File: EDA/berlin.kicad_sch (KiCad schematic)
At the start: 615 parts, among them J1 TYPE-C-31-M12_13, J2 Conn_ARM_JTAG_SWD_10, SW1,1 Rotary_Encoder_Switch_Chassis, SW1,10 MXSwitch, SW1,11 MXSwitch, SW1,12 MXSwitch, SW1,13 MXSwitch, SW1,14 MXSwitch, SW1,15 MXSwitch, SW1,16 Rotary_Encoder_Switch_Chassis, SW1,2 MXSwitch, SW1,3 MXSwitch, SW1,4 MXSwitch, SW1,5 MXSwitch, SW1,6 MXSwitch, SW1,7 MXSwitch, SW1,8 MXSwitch, SW1,9 MXSwitch, SW2,1 MXSwitch, SW2,10 MXSwitch, SW2,11 MXSwitch, SW2,12 MXSwitch, SW2,13 MXSwitch, SW2,14 MXSwitch, SW2,15 MXSwitch, SW2,16 MXSwitch, SW2,17 MXSwitch, SW2,18 MXSwitch, SW2,19 MXSwitch, SW2,2 MXSwitch, SW2,3 MXSwitch, SW2,4 MXSwitch, SW2,5 MXSwitch, SW2,6 MXSwitch, SW2,7 MXSwitch, SW2,9 MXSwitch, SW20-7,3 MXSwitch, SW3,1 MXSwitch, SW3,10 MXSwitch, SW3,11 MXSwitch, SW3,12 MXSwitch, SW3,13 MXSwitch, SW3,14 MXSwitch, SW3,15 MXSwitch, SW3,16 MXSwitch, SW3,17 MXSwitch, SW3,18 MXSwitch, SW3,19 MXSwitch, SW3,2 MXSwitch, SW3,3 MXSwitch, SW3,4 MXSwitch, SW3,5 MXSwitch, SW3,6 MXSwitch, SW3,7 MXSwitch, SW3,8 MXSwitch, SW3,9 MXSwitch, SW39-7,6 MXSwitch, SW4,1 MXSwitch, SW4,10 MXSwitch, SW4,11 MXSwitch, SW4,12 MXSwitch, SW4,13 MXSwitch, SW4,14 MXSwitch, SW4,15 MXSwitch, SW4,16 MXSwitch, SW4,17 MXSwitch, SW4,18 MXSwitch, SW4,19 MXSwitch, SW4,2 MXSwitch, SW4,3 MXSwitch, SW4,4 MXSwitch, SW4,5 MXSwitch, SW4,6 MXSwitch, SW4,7 MXSwitch, SW4,8 MXSwitch, SW4,9 MXSwitch, SW5,1 MXSwitch, SW5,10 MXSwitch, SW5,11 MXSwitch, SW5,12 MXSwitch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

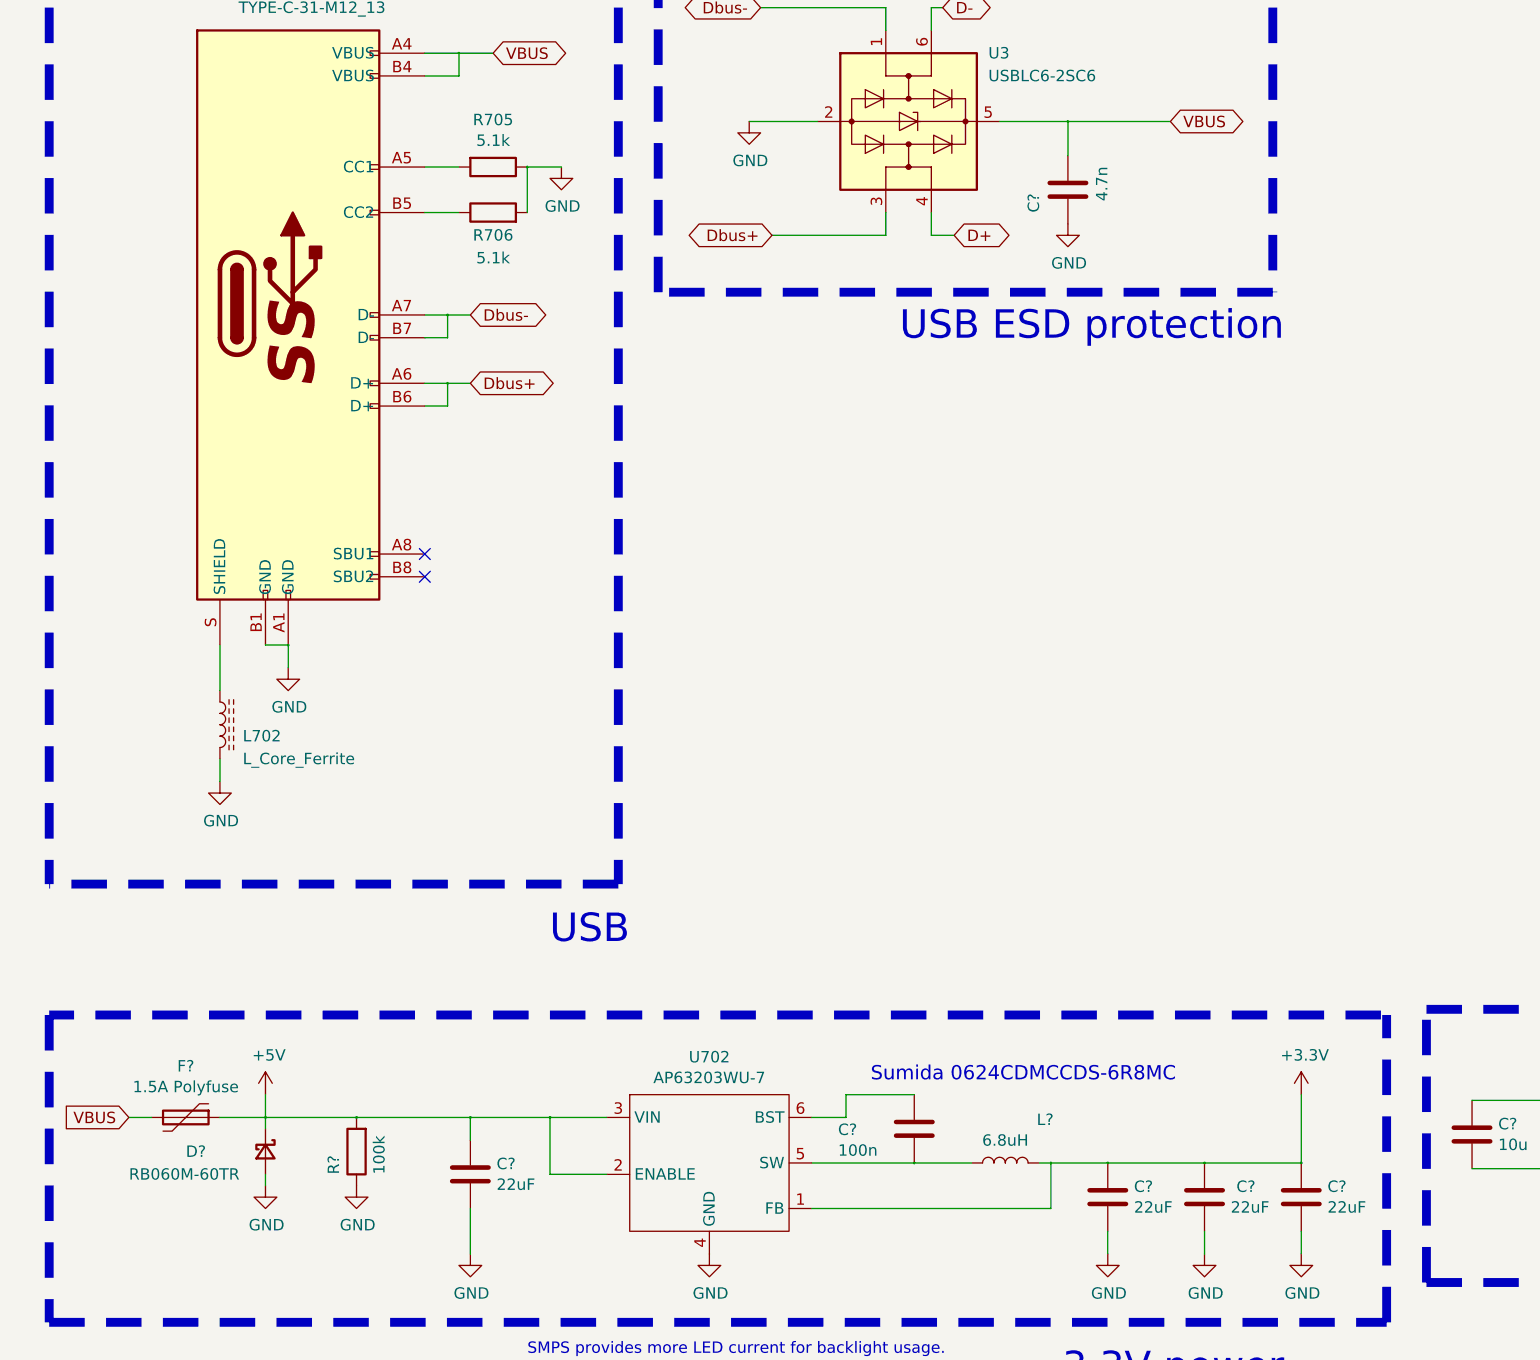
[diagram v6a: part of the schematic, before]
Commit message: Insert auxiliary components for ICs
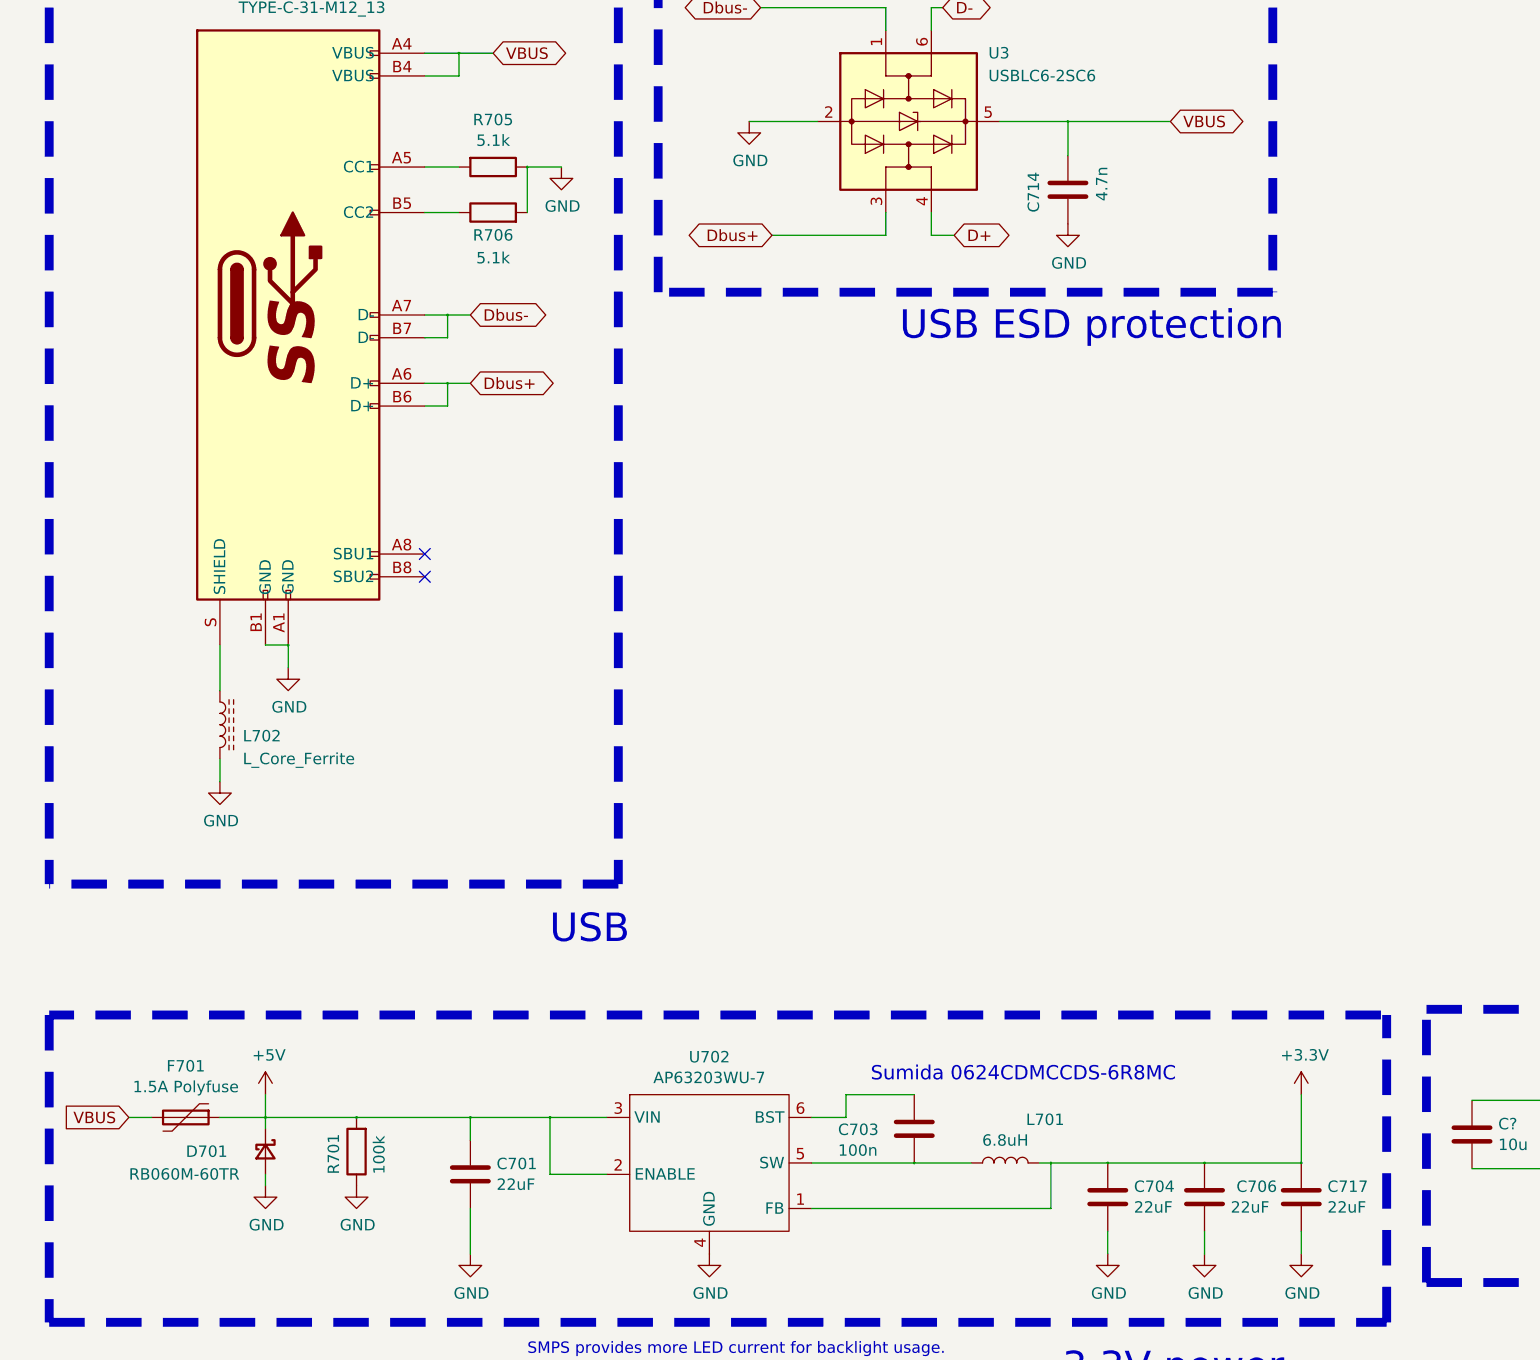
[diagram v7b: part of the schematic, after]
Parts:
- gave numbers to parts that had none: 10
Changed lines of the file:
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@@
   (symbol (lib_id "Device:L") (at 869.95 154.305 90) (unit 1)
     (in_bom yes) (on_board yes)
-    (property "Reference" "L?" (id 0) (at 874.395 149.479 90))
+    (property "Reference" "L701" (id 0) (at 874.395 149.479 90))
     (property "Value" "6.8uH" (id 1) (at 869.95 151.7904 90))
     (property "Footprint" "SumidaInductor:Sumida0624CDMCC" (id 2) (at 869.95 154.305 0)
@@
   (symbol (lib_id "Device:D_Schottky_Small") (at 787.4 153.035 270) (unit 1)
     (in_bom yes) (on_board yes)
-    (property "Reference" "D?" (id 0) (at 778.51 153.035 90)
+    (property "Reference" "D701" (id 0) (at 778.51 153.035 90)
       (effects (font (size 1.27 1.27)) (justify left))
     )
@@
   (symbol (lib_id "Device:R") (at 797.56 153.035 180) (unit 1)
     (in_bom yes) (on_board yes)
-    (property "Reference" "R?" (id 0) (at 795.02 155.575 90)
+    (property "Reference" "R701" (id 0) (at 795.02 155.575 90)
       (effects (font (size 1.27 1.27)) (justify right))
     )
@@
   (symbol (lib_id "Device:Polyfuse") (at 778.51 149.225 270) (unit 1)
     (in_bom yes) (on_board yes)
-    (property "Reference" "F?" (id 0) (at 778.51 143.51 90))
+    (property "Reference" "F701" (id 0) (at 778.51 143.51 90))
     (property "Value" "1.5A Polyfuse" (id 1) (at 778.51 145.8214 90))
     (property "Footprint" "Fuse:Fuse_1812_4532Metric_Pad1.30x3.40mm_HandSolder" (id 2) (at 773.43 150.495 0)
@@
   (symbol (lib_id "Device:C") (at 810.26 155.575 0) (unit 1)
     (in_bom yes) (on_board yes)
-    (property "Reference" "C?" (id 0) (at 813.181 154.4066 0)
+    (property "Reference" "C701" (id 0) (at 813.181 154.4066 0)
       (effects (font (size 1.27 1.27)) (justify left))
     )
@@
   (symbol (lib_id "Device:C") (at 859.79 150.495 0) (unit 1)
     (in_bom yes) (on_board yes)
-    (property "Reference" "C?" (id 0) (at 851.281 150.5966 0)
+    (property "Reference" "C703" (id 0) (at 851.281 150.5966 0)
       (effects (font (size 1.27 1.27)) (justify left))
     )
@@
   (symbol (lib_id "Device:C") (at 876.935 45.72 0) (unit 1)
     (in_bom yes) (on_board yes)
-    (property "Reference" "C?" (id 0) (at 873.125 48.26 90)
+    (property "Reference" "C714" (id 0) (at 873.125 48.26 90)
       (effects (font (size 1.27 1.27)) (justify left))
     )
@@
   (symbol (lib_id "Device:C") (at 881.38 158.115 0) (unit 1)
     (in_bom yes) (on_board yes)
-    (property "Reference" "C?" (id 0) (at 884.301 156.9466 0)
+    (property "Reference" "C704" (id 0) (at 884.301 156.9466 0)
       (effects (font (size 1.27 1.27)) (justify left))
     )
@@
   (symbol (lib_id "Device:C") (at 892.175 158.115 0) (unit 1)
     (in_bom yes) (on_board yes)
-    (property "Reference" "C?" (id 0) (at 895.731 156.9466 0)
+    (property "Reference" "C706" (id 0) (at 895.731 156.9466 0)
       (effects (font (size 1.27 1.27)) (justify left))
     )
@@
   (symbol (lib_id "Device:C") (at 902.97 158.115 0) (unit 1)
     (in_bom yes) (on_board yes)
-    (property "Reference" "C?" (id 0) (at 905.891 156.9466 0)
+    (property "Reference" "C717" (id 0) (at 905.891 156.9466 0)
       (effects (font (size 1.27 1.27)) (justify left))
     )
@@
       (reference "#PWR?") (unit 1) (value "GND") (footprint "")
     )
+    (path "/dfdf57f2-2cb8-4328-9440-eb9b1717e2b3"
+      (reference "C701") (unit 1) (value "22uF") (footprint "Capacitor_SMD:C_1206_3216Metric_Pad1.42x1.75mm_HandSolder")
+    )
+    (path "/83a0c1b0-7cee-4979-a4f9-8a4c9d4340cd"
+      (reference "C703") (unit 1) (value "100n") (footprint "Capacitor_SMD:C_0805_2012Metric_Pad1.15x1.40mm_HandSolder")
+    )
+    (path "/3eec4cef-8cd1-4b96-967e-b06039b64a20"
+      (reference "C704") (unit 1) (value "22uF") (footprint "Capacitor_SMD:C_1206_3216Metric_Pad1.42x1.75mm_HandSolder")
+    )
+    (path "/1157579c-3f84-4a9e-a7ba-522bb7b963bc"
+      (reference "C706") (unit 1) (value "22uF") (footprint "Capacitor_SMD:C_1206_3216Metric_Pad1.42x1.75mm_HandSolder")
+    )
+    (path "/8c11f89b-08b5-4aec-8104-98c04a450db2"
+      (reference "C714") (unit 1) (value "4.7n") (footprint "Capacitor_SMD:C_0805_2012Metric_Pad1.15x1.40mm_HandSolder")
+    )
+    (path "/9d44c771-d579-4696-ab84-f8105324921f"
+      (reference "C717") (unit 1) (value "22uF") (footprint "Capacitor_SMD:C_1206_3216Metric_Pad1.42x1.75mm_HandSolder")
+    )
     (path "/005dfdcf-d7ee-4caa-b732-20512abe6564"
       (reference "C?") (unit 1) (value "10u") (footprint "Capacitor_SMD:C_1206_3216Metric_Pad1.42x1.75mm_HandSolder")
@@
       (reference "C?") (unit 1) (value "100nF") (footprint "Capacitor_SMD:C_0805_2012Metric_Pad1.15x1.40mm_HandSolder")
     )
-    (path "/1157579c-3f84-4a9e-a7ba-522bb7b963bc"
-      (reference "C?") (unit 1) (value "22uF") (footprint "Capacitor_SMD:C_1206_3216Metric_Pad1.42x1.75mm_HandSolder")
-    )
     (path "/1c15df82-02ec-4fc7-9b02-d0cd59721543"
       (reference "C?") (unit 1) (value "10u") (footprint "Capacitor_SMD:C_1206_3216Metric_Pad1.42x1.75mm_HandSolder")
@@
       (reference "C?") (unit 1) (value "100nF") (footprint "Capacitor_SMD:C_0805_2012Metric_Pad1.15x1.40mm_HandSolder")
     )
-    (path "/3eec4cef-8cd1-4b96-967e-b06039b64a20"
-      (reference "C?") (unit 1) (value "22uF") (footprint "Capacitor_SMD:C_1206_3216Metric_Pad1.42x1.75mm_HandSolder")
-    )
     (path "/3fb3ab10-bc55-460e-b6f0-29a18e43e0ee"
       (reference "C?") (unit 1) (value "10u") (footprint "Capacitor_SMD:C_1206_3216Metric_Pad1.42x1.75mm_HandSolder")
@@
       (reference "C?") (unit 1) (value "100nF") (footprint "Capacitor_SMD:C_0805_2012Metric_Pad1.15x1.40mm_HandSolder")
     )
-    (path "/83a0c1b0-7cee-4979-a4f9-8a4c9d4340cd"
-      (reference "C?") (unit 1) (value "100n") (footprint "Capacitor_SMD:C_0805_2012Metric_Pad1.15x1.40mm_HandSolder")
-    )
     (path "/88ffa26b-513e-4201-ab97-c9a74cf6aca1"
       (reference "C?") (unit 1) (value "100n") (footprint "Capacitor_SMD:C_0805_2012Metric_Pad1.15x1.40mm_HandSolder")
     )
-    (path "/8c11f89b-08b5-4aec-8104-98c04a450db2"
-      (reference "C?") (unit 1) (value "4.7n") (footprint "Capacitor_SMD:C_0805_2012Metric_Pad1.15x1.40mm_HandSolder")
-    )
     (path "/9082253d-68b1-473a-88f7-1638236ae88a"
       (reference "C?") (unit 1) (value "100nF") (footprint "Capacitor_SMD:C_0805_2012Metric_Pad1.15x1.40mm_HandSolder")
@@
       (reference "C?") (unit 1) (value "100n") (footprint "Capacitor_SMD:C_0805_2012Metric_Pad1.15x1.40mm_HandSolder")
     )
-    (path "/9d44c771-d579-4696-ab84-f8105324921f"
-      (reference "C?") (unit 1) (value "22uF") (footprint "Capacitor_SMD:C_1206_3216Metric_Pad1.42x1.75mm_HandSolder")
-    )
     (path "/a0dced1a-6d0c-41dc-8e02-eb686969a275"
       (reference "C?") (unit 1) (value "10u") (footprint "Capacitor_SMD:C_1206_3216Metric_Pad1.42x1.75mm_HandSolder")
@@
       (reference "C?") (unit 1) (value "100nF") (footprint "Capacitor_SMD:C_0805_2012Metric_Pad1.15x1.40mm_HandSolder")
     )
-    (path "/dfdf57f2-2cb8-4328-9440-eb9b1717e2b3"
-      (reference "C?") (unit 1) (value "22uF") (footprint "Capacitor_SMD:C_1206_3216Metric_Pad1.42x1.75mm_HandSolder")
-    )
     (path "/e3c2cf99-ff58-4cc3-bcdb-1b334a4a78ad"
       (reference "C?") (unit 1) (value "100n") (footprint "Capacitor_SMD:C_0805_2012Metric_Pad1.15x1.40mm_HandSolder")
@@
       (reference "D7") (unit 1) (value "1N4148") (footprint "acheronComponents:D_SOD-123")
     )
+    (path "/59d78aa9-064a-494e-81ef-29cddf412066"
+      (reference "D701") (unit 1) (value "RB060M-60TR") (footprint "acheronComponents:D_SOD-123")
+    )
     (path "/01411503-47d2-4625-8a9f-54c36f67c49d"
       (reference "D?") (unit 1) (value "1N4148") (footprint "acheronComponents:D_SOD-123")
@@
       (reference "D?") (unit 1) (value "1N4148") (footprint "acheronComponents:D_SOD-123")
     )
-    (path "/59d78aa9-064a-494e-81ef-29cddf412066"
-      (reference "D?") (unit 1) (value "RB060M-60TR") (footprint "acheronComponents:D_SOD-123")
-    )
     (path "/5c728750-b5da-49e3-9aaf-1900031651ba"
       (reference "D?") (unit 1) (value "1N4148") (footprint "acheronComponents:D_SOD-123")
@@
     )
     (path "/e344eb22-37ed-45d9-9b96-b6364bbbd844"
-      (reference "F?") (unit 1) (value "1.5A Polyfuse") (footprint "Fuse:Fuse_1812_4532Metric_Pad1.30x3.40mm_HandSolder")
+      (reference "F701") (unit 1) (value "1.5A Polyfuse") (footprint "Fuse:Fuse_1812_4532Metric_Pad1.30x3.40mm_HandSolder")
     )
     (path "/8061ecd2-b448-4175-bfb2-5bc2273e1626"
@@
       (reference "J2") (unit 1) (value "Conn_ARM_JTAG_SWD_10") (footprint "Connector_PinSocket_2.54mm:PinSocket_2x05_P2.54mm_Vertical")
     )
+    (path "/81119b09-c2f2-4eb0-bbce-c0f875f0ffe7"
+      (reference "L701") (unit 1) (value "6.8uH") (footprint "SumidaInductor:Sumida0624CDMCC")
+    )
     (path "/455c4cbb-3d0b-48d2-aa90-82ba22ea7714"
       (reference "L702") (unit 1) (value "L_Core_Ferrite") (footprint "Inductor_SMD:L_0805_2012Metric_Pad1.15x1.40mm_HandSolder")
     )
-    (path "/81119b09-c2f2-4eb0-bbce-c0f875f0ffe7"
-      (reference "L?") (unit 1) (value "6.8uH") (footprint "SumidaInductor:Sumida0624CDMCC")
-    )
     (path "/87bed887-4561-4d19-8e44-a1cfedaafa26"
       (reference "L?") (unit 1) (value "L_Core_Ferrite") (footprint "Inductor_SMD:L_0805_2012Metric_Pad1.15x1.40mm_HandSolder")
@@
       (reference "Q?") (unit 1) (value "AO4406AL") (footprint "acheronComponents:SOIC-8")
     )
+    (path "/5ae093f6-285f-442e-a701-16cac7ddec9c"
+      (reference "R701") (unit 1) (value "100k") (footprint "Resistor_SMD:R_0805_2012Metric_Pad1.15x1.40mm_HandSolder")
+    )
     (path "/428cb4ff-8001-4f58-9763-4c9d4bfa8d79"
       (reference "R705") (unit 1) (value "5.1k") (footprint "Resistor_SMD:R_0805_2012Metric_Pad1.15x1.40mm_HandSolder")
@@
       (reference "R?") (unit 1) (value "100 1%") (footprint "Resistor_SMD:R_0805_2012Metric_Pad1.15x1.40mm_HandSolder")
     )
-    (path "/5ae093f6-285f-442e-a701-16cac7ddec9c"
-      (reference "R?") (unit 1) (value "100k") (footprint "Resistor_SMD:R_0805_2012Metric_Pad1.15x1.40mm_HandSolder")
-    )
     (path "/5b39e038-5457-4a32-a14f-eb27271ae23c"
